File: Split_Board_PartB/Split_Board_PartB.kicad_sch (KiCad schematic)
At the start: 0 parts

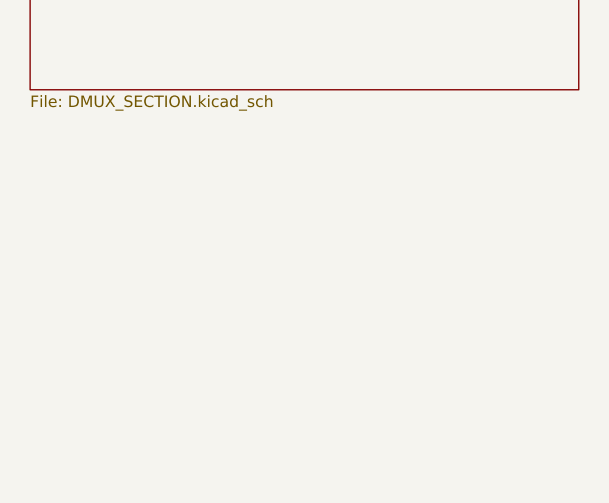
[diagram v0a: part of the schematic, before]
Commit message: added a adapter board in part b and edited the db37 connector in part A
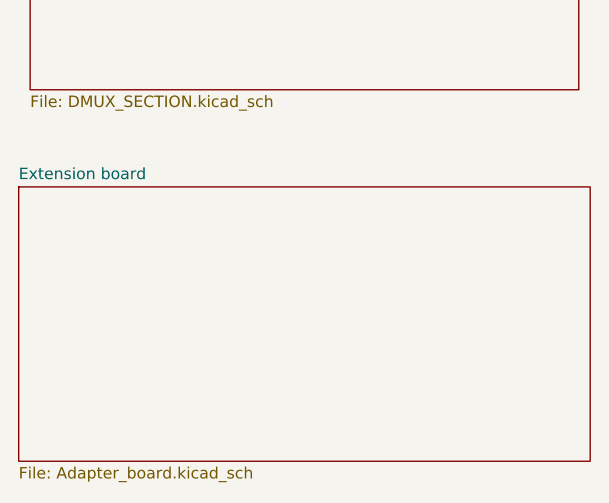
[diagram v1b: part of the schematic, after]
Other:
- added sheet Extension board (Adapter_board.kicad_sch)
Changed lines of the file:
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@@
     (rev "1")
+  )
+  (sheet (at 90.17 223.52) (size 63.5 30.48) (fields_autoplaced)
+    (stroke (width 0.1524) (type solid))
+    (fill (color 0 0 0 0.0000))
+    (property "Sheetname" "Extension board" (at 90.17 222.8084 0)
+      (effects (font (size 1.27 1.27)) (justify left bottom))
+    )
+    (property "Sheetfile" "Adapter_board.kicad_sch" (at 90.17 254.5846 0)
+      (effects (font (size 1.27 1.27)) (justify left top))
+    )
+    (instances
+      (project "Split_Board_PartB"
+        (path "/e2d56ecd-77dd-4fed-8d81-4a7d32aa0989" (page "5"))
+      )
+    )
   )
   (sheet (at 91.44 182.245) (size 60.96 30.48) (fields_autoplaced)
